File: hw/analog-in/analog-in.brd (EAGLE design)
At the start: 90.2 x 37 mm, 120 parts

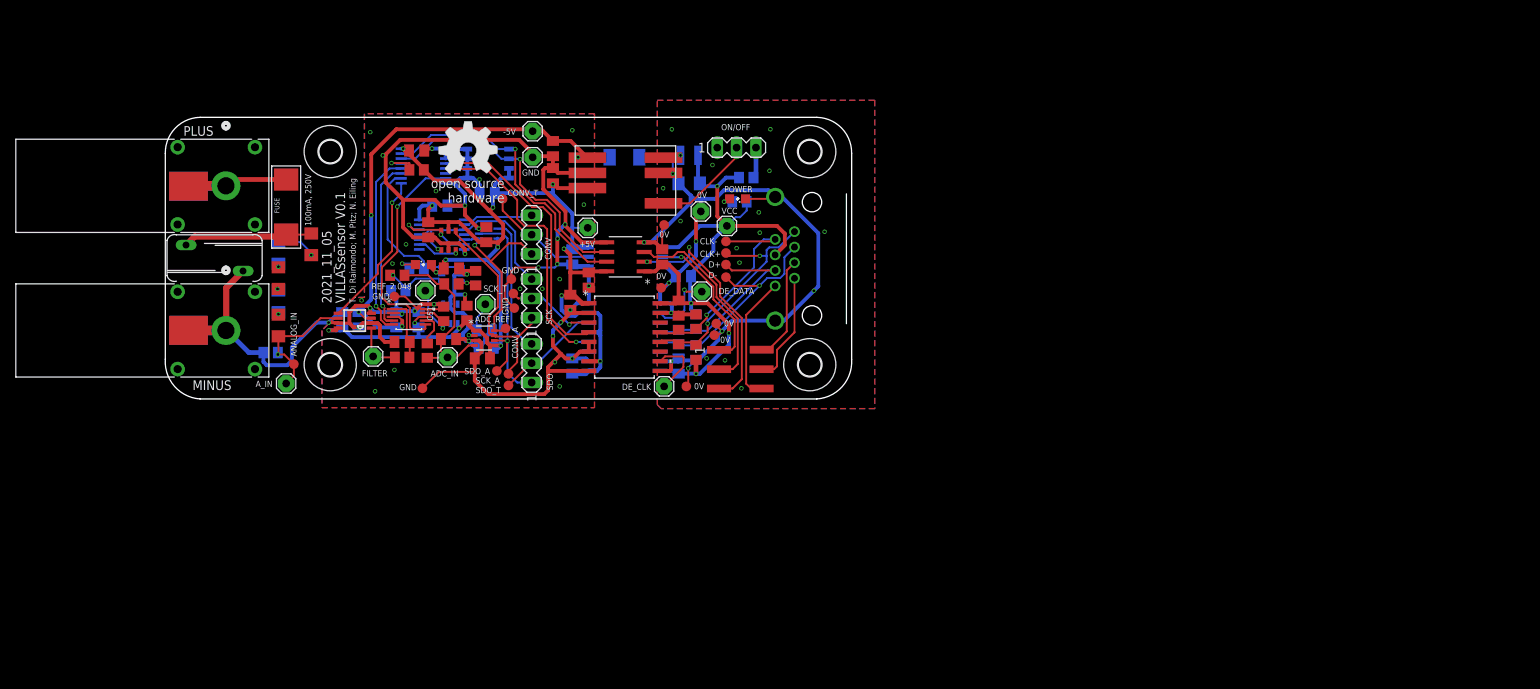
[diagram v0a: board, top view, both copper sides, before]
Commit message: hw/analog-in: fix mistakes from rev 1
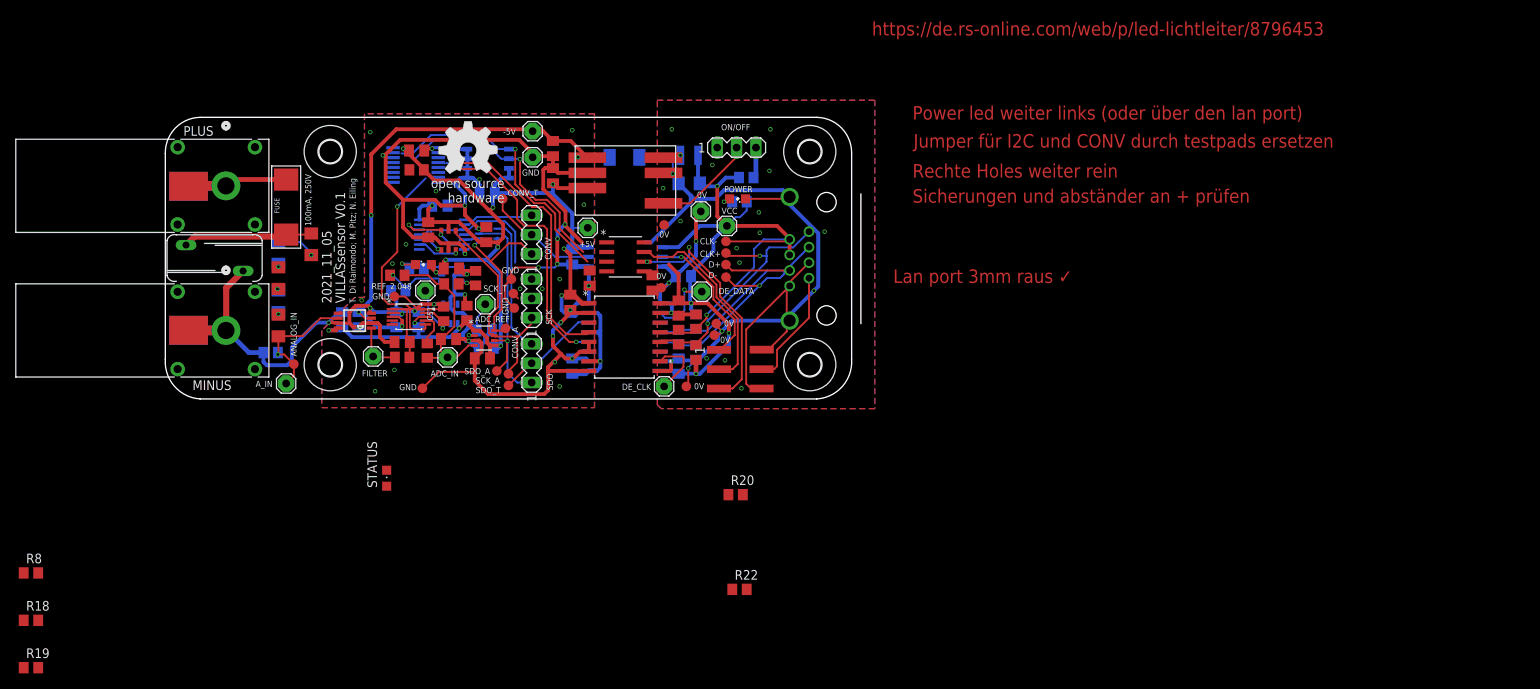
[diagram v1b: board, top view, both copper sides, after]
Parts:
- removed SHIFT_REGISTER: TCA9534ADWT, TCA9534ADWT:PW16_TEX
- added R18, R19: 1.6k, resistor:R0805
- added R20, R22: DNP, resistor:R0805
- added R8: 680, resistor:R0805
- added STATUS: GREEN, led:CHIPLED_0805
- added U$2: TCA9534, parts:TSSOP16L
- DC-DC_CONVERTER: value TDN_3-1211WI -> TDN 3-1221WISM
- I2C: value ADUM1251 -> ADUM1250
- INSTR_AMP: device AD8250:RM_10_ADI -> parts:RM_10_ADI
- LED2: value gr -> GREEN
- moved C12 9.93 mm to (57.8, 15.9)
- moved C6 8.39 mm to (66.0, 15.2)
- moved RJ45 1.91 mm to (88.9, 18.4)
- turned I2C to 0 degrees
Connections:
- removed net DIR_0: SERIAL_CLOCK.4, SHIFT_REGISTER.4
- removed net DIR_1: SERIAL_DATA.4, SHIFT_REGISTER.5
- removed net DIR_2: SHIFT_REGISTER.6
- removed net N$28: SCK.2, SCK_T.TP, SERIAL_CLOCK.3
- removed net P4: SHIFT_REGISTER.9, U$20.5
- removed net P5: R3.1, SATURATION_DETECT.1, SATURATION_DETECT.6, SHIFT_REGISTER.10
- removed net P6: INSTR_AMP.4, SHIFT_REGISTER.11
- removed net P7: INSTR_AMP.5, SHIFT_REGISTER.12
- removed net WR: INSTR_AMP.6, SHIFT_REGISTER.7
- new net CLK_DIR: SERIAL_CLOCK.4, U$2.4
- new net DATA_DIR: SERIAL_DATA.4, U$2.5
- new net GAIN_LSB: INSTR_AMP.4, U$2.11
- new net GAIN_MSB: INSTR_AMP.5, U$2.12
- new net INPUT_ZERO: U$2.9, U$20.5
- new net N$26: R8.2, STATUS.C
- new net N_STATUS_LED: R8.1, U$2.6
- new net N_WE: INSTR_AMP.6, U$2.7
- new net SAT_DETECT: R3.1, SATURATION_DETECT.1, SATURATION_DETECT.6, U$2.10
- net +5V: now also C12.1, FLIP-FLOP.1, FLIP-FLOP.10, FLIP-FLOP.13, FLIP-FLOP.4, I2C.1, R18.2, R19.2, STATUS.A, U$2.16; no longer C6.1, I2C.8, SHIFT_REGISTER.16
- net 0V: now also C6.2, I2C.5; no longer C12.2, I2C.4
- net DGND: now also C12.2, I2C.4, INSTR_AMP.1, U$2.1, U$2.2, U$2.3, U$2.8; no longer C6.2, I2C.5, INSTR_AMP.10, SHIFT_REGISTER.1, SHIFT_REGISTER.2, SHIFT_REGISTER.3, SHIFT_REGISTER.8
- net N$13: now also 74LVC1G11.4; no longer 74LVC1G11.1, FLIP-FLOP.11, FLIP-FLOP.3
- net N$15: now also INSTR_AMP.10; no longer INSTR_AMP.1
- net N$17: now also SATURATION_DETECT.4; no longer SATURATION_DETECT.3
- net N$18: now also SATURATION_DETECT.3; no longer SATURATION_DETECT.4
- net N$2: now also U$2.13; no longer SHIFT_REGISTER.13
- net N$4: now also I2C.3, R18.1, U$2.14; no longer I2C.6, SHIFT_REGISTER.14
- net N$6: now also I2C.2, R19.1, U$2.15; no longer I2C.7, SHIFT_REGISTER.15
- net SCK_ADC: now also 74LVC1G11.1, FLIP-FLOP.11, FLIP-FLOP.3, SCK.2, SCK_T.TP, SERIAL_CLOCK.3; no longer 74LVC1G11.4
- net SCL>: now also I2C.6, R22.1; no longer I2C.3
- net SDO>: now also I2C.7, R20.1; no longer I2C.2
- net V+: now also C6.1, I2C.8, R20.2, R22.2; no longer C12.1, I2C.1
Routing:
- net DIR_1: track 36.7 -> 0.00 mm, vias 2 -> 0
- net DATA_DIR: track 0.00 -> 36.6 mm, vias 0 -> 2
- net DIR_0: track 36.2 -> 0.00 mm, vias 1 -> 0
- net CLK_DIR: track 0.00 -> 36.1 mm, vias 0 -> 1
- net WR: track 30.2 -> 0.00 mm, vias 1 -> 0
- net N_WE: track 0.00 -> 27.5 mm, vias 0 -> 1
- net N$13: track 24.4 -> 0.00 mm, vias 1 -> 0
- net P7: track 24.2 -> 0.00 mm, vias 1 -> 0
- net P6: track 22.2 -> 0.00 mm, vias 1 -> 0
- net P5: track 21.1 -> 0.00 mm
- net SCK_ADC: track 28.9 -> 50.0 mm, vias 0 -> 1
- net P4: track 20.5 -> 0.00 mm, vias 1 -> 0
- net N$28: track 11.7 -> 0.00 mm, vias 1 -> 0
- net +5V: track 172.5 -> 167.2 mm
- net SAT_DETECT: track 0.00 -> 4.98 mm
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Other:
- board text added: "Jumper für I2C und CONV durch testpads ersetzen"
- board text added: "Lan port 3mm raus ✓"
- board text added: "Power led weiter links (oder über den lan port)"
- board text added: "Rechte Holes weiter rein"
- board text added: "Sicherungen und abständer an + prüfen"
- board text added: "https://de.rs-online.com/web/p/led-lichtleiter/8796453"

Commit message: ADC board fixes
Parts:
- removed PIN_HEADER_SMD: (no value), SMD10_2_pinheader:MA05-2
- added CONV1: PTR1B1,27, testpad:B1,27
- added POWER1: gr, led:SML0805
- added R23: 680, resistor:R0805
- moved R19 91.9 mm to (57.4, 20.4), turned to 90 degrees
- moved R18 86.5 mm to (55.2, 20.4), turned to 90 degrees
- moved R8 71.3 mm to (35.6, 26.8), turned to 180 degrees
- moved R22 42.2 mm to (70.5, 16.6)
- moved R20 34.4 mm to (71.1, 21.3), turned to 90 degrees
- moved STATUS 31.0 mm to (42.2, 18.5), turned to 180 degrees
- moved +5V 10.2 mm to (50.0, 29.5)
- moved C6 7.39 mm to (69.1, 22.0), turned to 90 degrees
- moved R5 5.89 mm to (17.7, 25.0), flipped to the bottom
- moved U$1 5.71 mm to (17.7, 31.2)
- moved GOLD_ORB_SM1 2.74 mm to (40.8, 30.1), turned to 180 degrees
- moved H1 2.70 mm to (84.0, 32.5)
- moved H2 2.70 mm to (84.0, 4.50)
- moved R_FILTER1 1.83 mm to (34.2, 6.99), turned to 270 degrees
- moved R12 1.44 mm to (43.8, 14.9), turned to 180 degrees
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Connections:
- removed net CONV<: PIN_HEADER_SMD.6, RJ45.5
- removed net CONV>: CONVERSION.2, PIN_HEADER_SMD.1
- removed net N_STATUS_LED: R8.1, U$2.6
- removed net SCL<: PIN_HEADER_SMD.5, RJ45.7
- removed net SCL>: I2C.6, PIN_HEADER_SMD.2, R22.1
- removed net SDO<: PIN_HEADER_SMD.4, RJ45.8
- removed net SDO>: I2C.7, PIN_HEADER_SMD.3, R20.1
- new net CONV: CONV1.TP, CONVERSION.2, RJ45.5
- new net N$22: R8.1, STATUS.A
- new net N$27: POWER1.A, R23.1
- new net SCL: I2C.6, R22.1, RJ45.7
- new net SDO: I2C.7, R20.1, RJ45.8
- new net STATUS_LED: R8.2, U$2.6
- net +5V: now also R23.2; no longer STATUS.A
- net DGND: now also POWER1.C, STATUS.C
- net N$26: now also ADC_.7, SCK.2, SCK_A.TP; no longer R8.2, STATUS.C
- net SCK_ADC: no longer ADC_.7, SCK.2, SCK_A.TP
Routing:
- net SDO>: track 31.1 -> 0.00 mm, vias 2 -> 0
- net SCL: track 0.00 -> 30.2 mm
- net +5V: track 167.2 -> 194.9 mm, vias 14 -> 18
- net CONV: track 0.00 -> 26.8 mm, vias 0 -> 1
- net SCL>: track 25.5 -> 0.00 mm
- net GAIN_MSB: track 0.00 -> 24.3 mm, vias 0 -> 1
- net SDO: track 0.00 -> 24.0 mm
- net GAIN_LSB: track 0.00 -> 23.2 mm, vias 0 -> 1
- net INPUT_ZERO: track 0.00 -> 21.7 mm, vias 0 -> 1
- net SAT_DETECT: track 4.98 -> 25.9 mm
- net N$22: track 0.00 -> 19.3 mm, vias 0 -> 2
- net CONV>: track 18.8 -> 0.00 mm, vias 1 -> 0
- net SDO<: track 17.5 -> 0.00 mm
- net SCL<: track 15.5 -> 0.00 mm
- net CONV<: track 14.5 -> 0.00 mm
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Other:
- board text added: "2022_10_08"
- board text added: "M. Pitz; N. Eiling"
- board text added: "OL"
- board text added: "PWR"
- board text added: "ST"
- board text added: "VILLASsensor V0.2"
- board text removed: "2021_11_05"
- board text removed: "T. Di Raimondo; M. Pitz; N. Eiling"
- board text removed: "VILLASsensor V0.1"

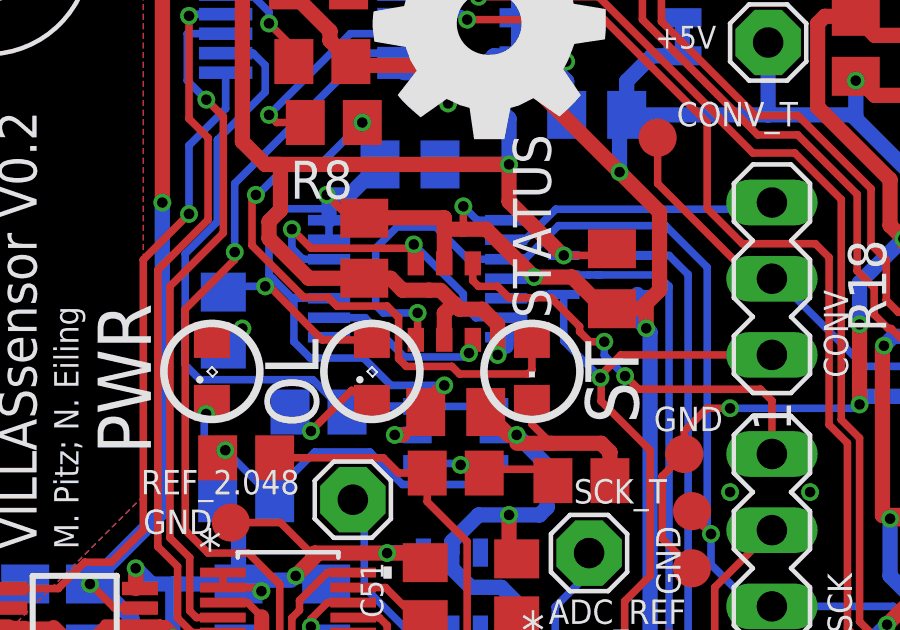
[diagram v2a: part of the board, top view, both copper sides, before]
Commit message: hw/analog-in: update schematics for analog in
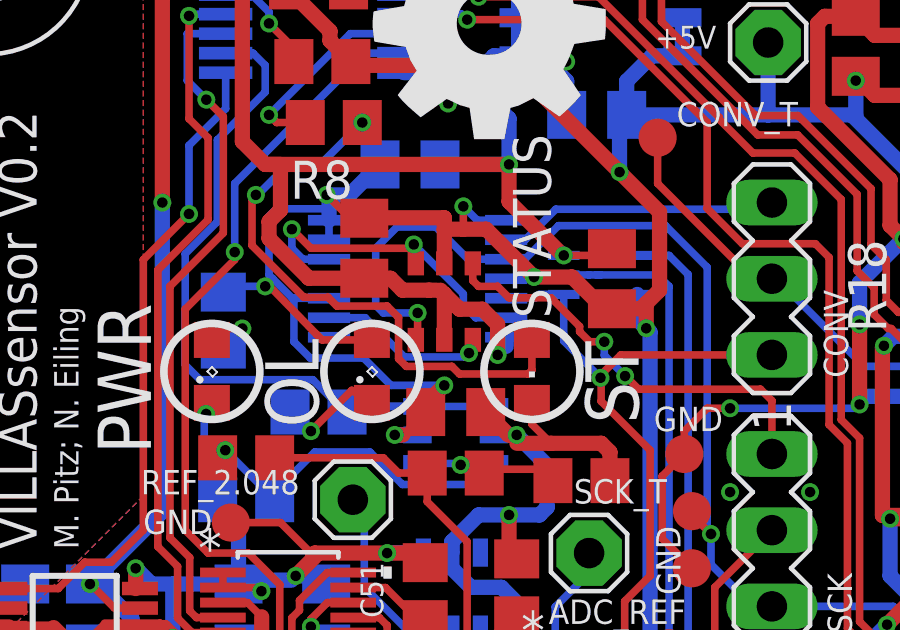
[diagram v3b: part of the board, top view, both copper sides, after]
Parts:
- R_FILTER1: value nb -> 0
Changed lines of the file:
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@@
 <drawing>
 <settings>
-<setting alwaysvectorfont="yes"/>
+<setting alwaysvectorfont="no"/>
 <setting verticaltext="up"/>
 </settings>
@@
 <layer number="14" name="Route14" color="22" fill="1" visible="no" active="no"/>
 <layer number="15" name="Route15" color="23" fill="1" visible="no" active="no"/>
-<layer number="16" name="Bottom" color="1" fill="1" visible="yes" active="yes"/>
+<layer number="16" name="Bottom" color="1" fill="1" visible="no" active="yes"/>
 <layer number="17" name="Pads" color="2" fill="1" visible="yes" active="yes"/>
 <layer number="18" name="Vias" color="2" fill="1" visible="yes" active="yes"/>
@@
 <layer number="20" name="Dimension" color="24" fill="1" visible="yes" active="yes"/>
 <layer number="21" name="tPlace" color="7" fill="1" visible="yes" active="yes"/>
-<layer number="22" name="bPlace" color="7" fill="1" visible="yes" active="yes"/>
+<layer number="22" name="bPlace" color="7" fill="1" visible="no" active="yes"/>
 <layer number="23" name="tOrigins" color="15" fill="1" visible="yes" active="yes"/>
-<layer number="24" name="bOrigins" color="15" fill="1" visible="yes" active="yes"/>
+<layer number="24" name="bOrigins" color="15" fill="1" visible="no" active="yes"/>
 <layer number="25" name="tNames" color="7" fill="1" visible="yes" active="yes"/>
-<layer number="26" name="bNames" color="7" fill="1" visible="yes" active="yes"/>
+<layer number="26" name="bNames" color="7" fill="1" visible="no" active="yes"/>
 <layer number="27" name="tValues" color="7" fill="1" visible="no" active="yes"/>
 <layer number="28" name="bValues" color="7" fill="1" visible="no" active="yes"/>
@@
 <layer number="38" name="bTest" color="7" fill="1" visible="no" active="yes"/>
 <layer number="39" name="tKeepout" color="4" fill="11" visible="yes" active="yes"/>
-<layer number="40" name="bKeepout" color="1" fill="11" visible="yes" active="yes"/>
+<layer number="40" name="bKeepout" color="1" fill="11" visible="no" active="yes"/>
 <layer number="41" name="tRestrict" color="4" fill="10" visible="yes" active="yes"/>
-<layer number="42" name="bRestrict" color="1" fill="10" visible="yes" active="yes"/>
+<layer number="42" name="bRestrict" color="1" fill="10" visible="no" active="yes"/>
 <layer number="43" name="vRestrict" color="2" fill="10" visible="no" active="yes"/>
 <layer number="44" name="Drills" color="7" fill="1" visible="no" active="yes"/>
@@
 <layer number="50" name="dxf" color="7" fill="1" visible="no" active="no"/>
 <layer number="51" name="tDocu" color="7" fill="1" visible="yes" active="yes"/>
-<layer number="52" name="bDocu" color="7" fill="1" visible="yes" active="yes"/>
+<layer number="52" name="bDocu" color="7" fill="1" visible="no" active="yes"/>
 <layer number="53" name="tGND_GNDA" color="7" fill="9" visible="no" active="no"/>
 <layer number="54" name="bGND_GNDA" color="1" fill="9" visible="no" active="no"/>
@@
 <attribute name="VALUE" x="72.263" y="30.099" size="1.27" layer="27" ratio="10"/>
 </element>
-<element name="R_FILTER1" library="rcl" library_urn="urn:adsk.eagle:library:334" package="R0805" package3d_urn="urn:adsk.eagle:package:23553/2" value="nb" x="34.163" y="6.985" smashed="yes" rot="R270">
+<element name="R_FILTER1" library="rcl" library_urn="urn:adsk.eagle:library:334" package="R0805" package3d_urn="urn:adsk.eagle:package:23553/2" value="0" x="34.163" y="6.985" smashed="yes" rot="R270">
 <attribute name="DIGIKEY" value="P220DACT-ND" x="34.163" y="6.985" size="1.778" layer="27" rot="R270" display="off"/>
 <attribute name="NAME" x="35.433" y="9.144" size="0.762" layer="100" rot="R270"/>
@@
 <wire x1="39.116" y1="21.209" x2="38.735" y2="21.209" width="0.254" layer="1"/>
 <wire x1="40.513" y1="20.574" x2="39.751" y2="20.574" width="0.508" layer="1"/>
-<wire x1="39.751" y1="20.574" x2="39.5605" y2="20.7645" width="0.508" layer="1"/>
-<wire x1="39.5605" y1="20.7645" x2="39.116" y2="21.209" width="0.508" layer="1"/>
-<wire x1="39.243" y1="19.553" x2="39.243" y2="20.447" width="0.508" layer="1"/>
-<wire x1="39.243" y1="20.447" x2="39.5605" y2="20.7645" width="0.508" layer="1"/>
+<wire x1="39.751" y1="20.574" x2="39.243" y2="21.082" width="0.508" layer="1"/>
+<wire x1="39.243" y1="21.082" x2="39.116" y2="21.209" width="0.508" layer="1"/>
+<wire x1="39.243" y1="19.553" x2="39.243" y2="21.082" width="0.508" layer="1"/>
 <wire x1="31.496" y1="17.45" x2="31.50185" y2="17.27785" width="0.254" layer="1"/>
 <wire x1="31.50185" y1="17.27785" x2="31.3055" y2="17.0815" width="0.254" layer="1"/>

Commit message: hw: change isolator to si8400ab
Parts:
- I2C: value ADUM1250 -> SI8400AB-B-IS
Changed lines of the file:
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@@
 <attribute name="VENDOR" value="Traco Power" x="16.764" y="61.722" size="1.778" layer="27" rot="R180" display="off"/>
 </element>
-<element name="I2C" library="ADUM1251WARZ" package="R_8_ADI" value="ADUM1250" x="62.484" y="18.669" smashed="yes">
+<element name="I2C" library="ADUM1251WARZ" package="R_8_ADI" value="SI8400AB-B-IS" x="62.484" y="18.669" smashed="yes">
 <attribute name="BUILT_BY" value="EMA_UL_Team" x="113.284" y="-25.781" size="1.778" layer="27" display="off"/>
 <attribute name="COPYRIGHT" value="Copyright (C) 2018 Accelerated Designs. All rights reserved" x="113.284" y="-25.781" size="1.778" layer="27" display="off"/>
